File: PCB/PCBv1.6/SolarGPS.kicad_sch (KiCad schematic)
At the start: 46 parts, among them J1 Conn_01x10_Female, J2 Solar2+, J3 Solar1+, J4 GND, J5 GND, J6 Conn_02x03_Odd_Even, J7 Screw_Terminal_01x01, J8 Conn_01x04_Male, U1 BQ25505, U2 MAX-M10Q, U3 STM32L031G6Ux, U4 MAX40200AUK, U6 LIS3DH, Y1 32.768

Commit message: More Progress
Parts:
- removed D2: LED, Diode_SMD:D_0805_2012Metric, symbol Device:LED
- removed R2, R3: 100, Resistor_SMD:R_0603_1608Metric, symbol Device:R_Small
- removed U2: MAX-M10Q, RF_GPS:ublox_MAX, symbol RF_GPS:MAX-M8Q
- added U2: MAX-M10S, Margo_Lib:MAX-8, symbol MargoGeneral:MAX-M10S
- C8: symbol Device:CP -> Device:C_Polarized
- U1: footprint Package_DFN_QFN:QFN-20-1EP_3.5x3.5mm_P0.5mm_EP2x2mm -> Package_DFN_QFN:Texas_VQFN-RGR-20
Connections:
- net GND: now also U2.1 (GND), U2.10 (GND), U2.12 (GND)
- net GPS_EN: now also U3.10 (PA4); no longer U3.24 (PB3)
- net GPS_EXINT: now also U2.5 (EXINT)
- net GPS_RF: now also U2.11 (RF_IN)
- net GPS_UART_MISO: now also U2.2 (TXD)
- net GPS_UART_MOSI: now also U2.3 (RXD)
- net GPS_VDD: now also U2.7 (VCC_IO), U2.8 (VCC)
- net VBAT_OK: now also J1.5 (Pin_5)
- net VDD: now also U2.6 (V_BCKP)
- net DISPEN: no longer names the net of U3.18 (PA8)
- net DISPEN: no longer J1.5 (Pin_5)
- net LED: no longer names the net of U3.19 (PA9)
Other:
- note added: "Pin 5: LCD Enable"
- moved on the sheet: AE1, C1, C2, C5, J8, R4, U4

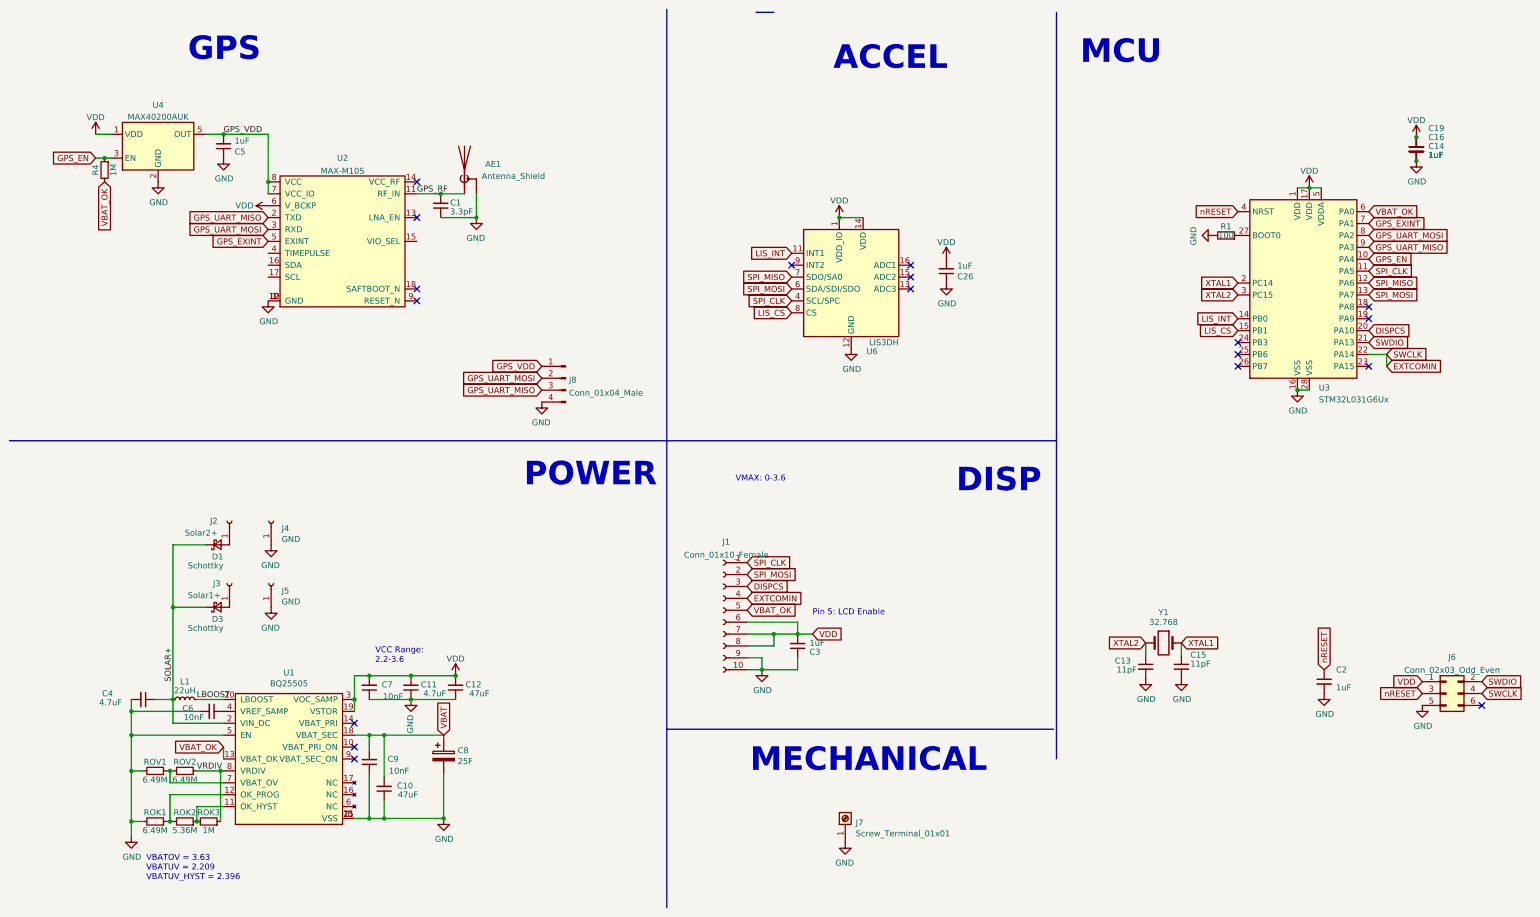
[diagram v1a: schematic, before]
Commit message: Replace GNSS with L96
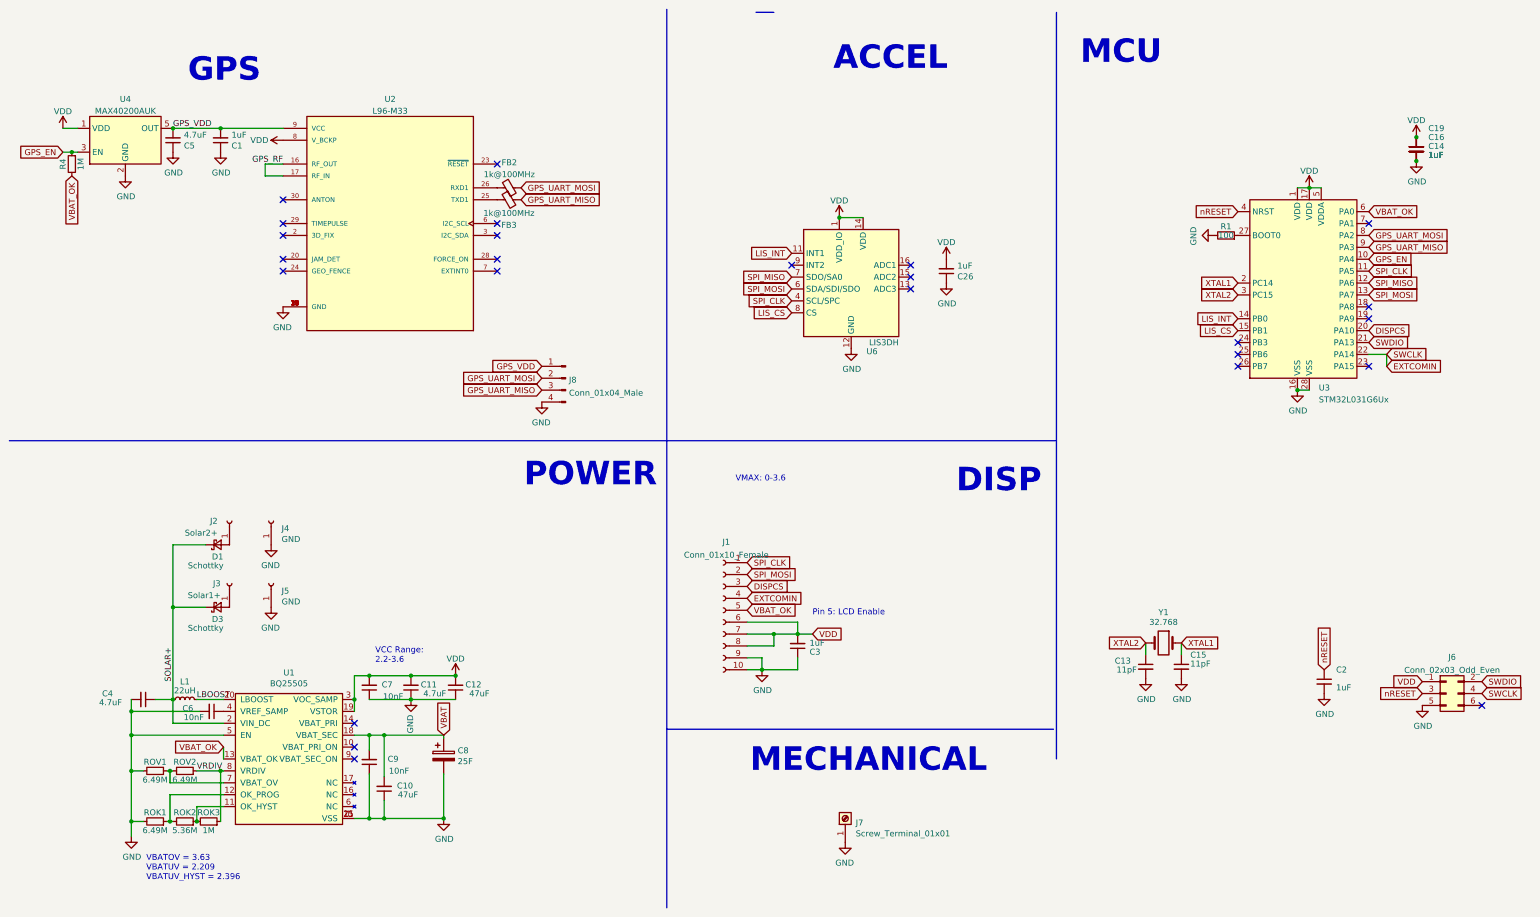
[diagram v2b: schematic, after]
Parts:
- removed AE1: Antenna_Shield, RF_Antenna:Pulse_W3011, symbol Device:Antenna_Shield
- removed U2: MAX-M10S, Margo_Lib:MAX-8, symbol MargoGeneral:MAX-M10S
- added FB2, FB3: 1k@100MHz, Resistor_SMD:R_0603_1608Metric, symbol Device:FerriteBead_Small
- added U2: L96-M33, XCVR_L96-M33, symbol Heliograph:L96-M33
- C1: value 3.3pF -> 1uF; footprint Capacitor_SMD:C_0402_1005Metric -> Capacitor_SMD:C_0603_1608Metric
- C5: value 1uF -> 4.7uF; footprint Capacitor_SMD:C_0603_1608Metric -> Capacitor_SMD:C_0805_2012Metric
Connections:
- net GND: now also U2.10 (GND), U2.11 (GND), U2.12 (GND), U2.13 (GND), U2.14 (GND), U2.15 (GND), U2.18 (GND), U2.19 (GND), U2.21 (GND), U2.22 (GND), U2.27 (GND), U2.31 (GND), U2.4 (GND), U2.5 (GND)
- net GPS_RF: now also U2.16 (RF_OUT), U2.17 (RF_IN); no longer C1.2
- net GPS_UART_MISO: now also FB3.2
- net GPS_UART_MOSI: now also FB2.1
- net GPS_VDD: now also C1.2, U2.9 (VCC)
- net VDD: now also U2.8 (V_BCKP)
- net GPS_EXINT: no longer names the net of U3.7 (PA1)
- new net: FB3.1, U2.25 (TXD1)
- new net: FB2.2, U2.26 (RXD1)
- no-connect marks 18 -> 25
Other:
- moved on the sheet: C5, R4, U4

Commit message: Update PCBV10
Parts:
- removed C11, C4: 4.7uF, Capacitor_SMD:C_0805_2012Metric, symbol Device:C_Small
- removed C12: 47uF, Capacitor_SMD:C_1206_3216Metric, symbol Device:C_Small
- removed C8: 25F, Heliograph:TPLC3R8-25MR8X20, symbol Device:C_Polarized
- removed D3: Schottky, Diode_SMD:D_SOD-323_HandSoldering, symbol Device:D_Schottky_Small
- removed ROK1, ROV1, ROV2: 6.49M, Resistor_SMD:R_0603_1608Metric, symbol Device:R_Small
- removed ROK2: 5.36M, Resistor_SMD:R_0603_1608Metric, symbol Device:R_Small
- removed ROK3: 1M, Resistor_SMD:R_0603_1608Metric, symbol Device:R_Small
- removed U1: BQ25505, Package_DFN_QFN:Texas_VQFN-RGR-20, symbol MargoGeneral:BQ25505
- added C4: 25F, Heliograph:TPLC3R8-25MR8X20, symbol Device:C_Polarized
- added C8: 10nF, Capacitor_SMD:C_0603_1608Metric, symbol Device:C_Small
- added D2: Schottky, Diode_SMD:D_SOD-323_HandSoldering, symbol Device:D_Schottky_Small
- added R2, R3: 1M, Resistor_SMD:R_0603_1608Metric, symbol Device:R_Small
- added R6: 432k, Resistor_SMD:R_0603_1608Metric, symbol Device:R_Small
- added R7: 86k, Resistor_SMD:R_0603_1608Metric, symbol Device:R_Small
- added U1: TPS63802, Margo_Lib:VREG_TPS63802DLAR, symbol SolarGPS-rescue:TPS63802-VeridianDesigns
- C6: value 10nF -> 1uF
- C7: value 10nF -> 0.1uF
- C9: value 10nF -> 47uF; footprint Capacitor_SMD:C_0603_1608Metric -> Capacitor_SMD:C_1206_3216Metric
- J2: value Solar2+ -> GND
- J3: value Solar1+ -> GND
- J4: value GND -> Solar1+
- J5: value GND -> Solar2+
- L1: value 22uH -> 0.47uH; footprint Heliograph:744031220 -> Inductor_SMD:L_0805_2012Metric_Pad1.05x1.20mm_HandSolder; Part 744031220 -> DFE201612E
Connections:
- net GND: now also C6.1, J2.1 (Pin_1), J3.1 (Pin_1), R4.2, C4.2, C8.1, R3.2, R7.1, U1.2 (MODE), U1.3 (AGND), U1.8 (GND); no longer C6.2, J4.1 (Pin_1), J5.1 (Pin_1)
- net VBAT: now also C6.2, D1.1 (K), C4.1, D2.1 (K), R2.1, U1.10 (VIN); no longer C9.2
- net VDD: now also C9.2, J1.5 (Pin_5), C8.2, R6.2, U1.6 (VOUT); no longer C7.2
- net VBATSENSE: now reaches U3.7 (PA1)
- net VBATSENSE: now also C7.2, R2.2, R3.1, U1.1 (EN)
- net SOLAR1+: now reaches D1.2 (A)
- net SOLAR1+: now also J4.1 (Pin_1); no longer J2.1 (Pin_1)
- net LBOOST: no longer names the net of L1.2
- net LBOOST: now also U1.7 (L2)
- net SOLAR+: no longer names the net of L1.1
- net SOLAR+: now also U1.9 (L1); no longer D1.1 (K)
- removed net VBAT_OK: J1.5 (Pin_5), R4.2, U3.6 (PA0)
- new net FB: R6.1, R7.2, U1.4 (FB)
- new net SOLAR2+: D2.2 (A), J5.1 (Pin_1)
- no-connect marks 25 -> 23
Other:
- note added: "VOUT = 3.01"
- note removed: "VBATOV = 3.63 VBATUV = 2.209 VBATUV_HYST = 2.396"
- note removed: "VCC Range: 2.2-3.6"
- note removed: "VMAX: 0-3.6"

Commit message: PCB1.6
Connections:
- net DISPCS: now also U3.19 (PA9); no longer U3.20 (PA10)
- net GND: now also J1.8 (Pin_8)
- net VDD: no longer J1.5 (Pin_5), J1.8 (Pin_8)
- net EXTCOMIN renamed SWCLK
- net SWCLK: no longer J1.4 (Pin_4)
- new net LCDEN: J1.5 (Pin_5), U3.20 (PA10)
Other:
- note added: "Pin 4: EXTIN Pin 5: LCD Enable Pin 8: EXTMODE H=Hardware, L=Software"
- note removed: "Pin 5: LCD Enable"
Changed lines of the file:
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@@
   (junction (at 66.04 153.035) (diameter 0) (color 0 0 0 0)
   )
-  (junction (at 180.34 142.24) (diameter 0) (color 0 0 0 0)
-  )
   (junction (at 57.15 36.83) (diameter 0) (color 0 0 0 0)
   )
@@
   (junction (at 85.09 163.195) (diameter 0) (color 0 0 0 0)
   )
+  (junction (at 172.72 149.86) (diameter 0) (color 0 0 0 0)
+  )
   (junction (at 66.04 165.735) (diameter 0) (color 0 0 0 0)
   )
@@
   (junction (at 119.38 165.735) (diameter 0) (color 0 0 0 0)
   )
-  (junction (at 175.26 144.78) (diameter 0) (color 0 0 0 0)
-  )
   (junction (at 46.99 46.99) (diameter 0) (color 0 0 0 0)
   )
-  (no_connect (at 302.26 77.47))
+  (no_connect (at 169.545 137.16))
   (no_connect (at 204.47 71.12))
   (no_connect (at 107.315 155.575))
@@
     (stroke (width 0) (type default) (color 0 0 0 0))
   )
-  (wire (pts (xy 180.34 139.7) (xy 169.545 139.7))
-    (stroke (width 0) (type default) (color 0 0 0 0))
-  )
   (wire (pts (xy 172.72 149.86) (xy 172.72 152.4))
     (stroke (width 0) (type default) (color 0 0 0 0))
@@
     (stroke (width 0) (type default) (color 0 0 0 0))
   )
-  (wire (pts (xy 175.26 147.32) (xy 175.26 144.78))
+  (wire (pts (xy 172.72 149.86) (xy 172.72 147.32))
     (stroke (width 0) (type default) (color 0 0 0 0))
   )
@@
     (stroke (width 0) (type default) (color 0 0 0 0))
   )
+  (wire (pts (xy 172.72 147.32) (xy 169.545 147.32))
+    (stroke (width 0) (type default) (color 0 0 0 0))
+  )
   (polyline (pts (xy 12.065 103.505) (xy 235.585 103.505))
     (stroke (width 0) (type default) (color 0 0 0 0))
@@
     (stroke (width 0) (type default) (color 0 0 0 0))
   )
-  (wire (pts (xy 169.545 147.32) (xy 175.26 147.32))
-    (stroke (width 0) (type default) (color 0 0 0 0))
-  )
   (wire (pts (xy 85.09 163.195) (xy 86.995 163.195))
     (stroke (width 0) (type default) (color 0 0 0 0))
@@
     (stroke (width 0) (type default) (color 0 0 0 0))
   )
-  (wire (pts (xy 169.545 144.78) (xy 175.26 144.78))
+  (wire (pts (xy 169.545 144.78) (xy 180.34 144.78))
     (stroke (width 0) (type default) (color 0 0 0 0))
   )
@@
     (stroke (width 0) (type default) (color 0 0 0 0))
   )
-  (wire (pts (xy 180.34 142.24) (xy 180.34 139.7))
-    (stroke (width 0) (type default) (color 0 0 0 0))
-  )
   (wire (pts (xy 25.4 46.99) (xy 36.83 46.99))
     (stroke (width 0) (type default) (color 0 0 0 0))
   )
-  (wire (pts (xy 175.26 144.78) (xy 180.34 144.78))
-    (stroke (width 0) (type default) (color 0 0 0 0))
-  )
   (wire (pts (xy 85.09 163.195) (xy 85.09 165.735))
     (stroke (width 0) (type default) (color 0 0 0 0))
@@
     (stroke (width 0) (type default) (color 0 0 0 0))
   )
-  (wire (pts (xy 302.26 85.09) (xy 306.07 85.09))
-    (stroke (width 0) (type default) (color 0 0 0 0))
-  )
   (wire (pts (xy 36.83 46.99) (xy 46.99 46.99))
     (stroke (width 0) (type default) (color 0 0 0 0))
@@
   )
   (wire (pts (xy 107.315 153.035) (xy 116.205 153.035))
-    (stroke (width 0) (type default) (color 0 0 0 0))
-  )
-  (wire (pts (xy 306.07 87.63) (xy 306.07 85.09))
     (stroke (width 0) (type default) (color 0 0 0 0))
   )
@@
     (effects (font (size 5.0038 5.0038) (thickness 1.0008) bold) (justify left bottom))
   )
-  (text "Pin 5: LCD Enable" (at 183.515 140.97 0)
+  (text "Pin 4: EXTIN\nPin 5: LCD Enable\nPin 8: EXTMODE H=Hardware, L=Software"
+    (at 189.23 138.43 0)
     (effects (font (size 1.27 1.27)) (justify left bottom))
   )
@@
     )
   )
+  (global_label "LCDEN" (shape input) (at 302.26 80.01 0) (fields_autoplaced)
+    (effects (font (size 1.27 1.27)) (justify left))
+    (property "Intersheet References" "${INTERSHEET_REFS}" (id 0) (at 310.6318 79.9306 0)
+      (effects (font (size 1.27 1.27)) (justify left) hide)
+    )
+  )
   (global_label "GPS_UART_MISO" (shape input) (at 121.285 52.07 0) (fields_autoplaced)
     (effects (font (size 1.27 1.27)) (justify left))
@@
     )
   )
-  (global_label "DISPCS" (shape input) (at 302.26 80.01 0) (fields_autoplaced)
-    (effects (font (size 1.27 1.27)) (justify left))
-    (property "Intersheet References" "${INTERSHEET_REFS}" (id 0) (at 311.418 79.9306 0)
+  (global_label "DISPCS" (shape input) (at 302.26 77.47 0) (fields_autoplaced)
+    (effects (font (size 1.27 1.27)) (justify left))
+    (property "Intersheet References" "${INTERSHEET_REFS}" (id 0) (at 311.418 77.3906 0)
       (effects (font (size 1.27 1.27)) (justify left) hide)
     )
@@
     )
   )
-  (global_label "EXTCOMIN" (shape input) (at 306.07 87.63 0) (fields_autoplaced)
-    (effects (font (size 1.27 1.27)) (justify left))
-    (property "Intersheet References" "${INTERSHEET_REFS}" (id 0) (at 317.7075 87.5506 0)
-      (effects (font (size 1.27 1.27)) (justify left) hide)
-    )
-  )
   (global_label "SWDIO" (shape input) (at 302.26 82.55 0) (fields_autoplaced)
     (effects (font (size 1.27 1.27)) (justify left))
@@
     )
   )
-  (global_label "EXTCOMIN" (shape input) (at 169.545 137.16 0) (fields_autoplaced)
-    (effects (font (size 1.27 1.27)) (justify left))
-    (property "Intersheet References" "${INTERSHEET_REFS}" (id 0) (at 181.1825 137.0806 0)
-      (effects (font (size 1.27 1.27)) (justify left) hide)
-    )
-  )
   (global_label "SPI_MOSI" (shape input) (at 169.545 132.08 0) (fields_autoplaced)
     (effects (font (size 1.27 1.27)) (justify left))
@@
     )
   )
-  (global_label "SWCLK" (shape input) (at 306.07 85.09 0) (fields_autoplaced)
-    (effects (font (size 1.27 1.27)) (justify left))
-    (property "Intersheet References" "${INTERSHEET_REFS}" (id 0) (at 314.6232 85.0106 0)
+  (global_label "SWCLK" (shape input) (at 302.26 85.09 0) (fields_autoplaced)
+    (effects (font (size 1.27 1.27)) (justify left))
+    (property "Intersheet References" "${INTERSHEET_REFS}" (id 0) (at 310.8132 85.0106 0)
       (effects (font (size 1.27 1.27)) (justify left) hide)
     )
@@
     (property "Intersheet References" "${INTERSHEET_REFS}" (id 0) (at 246.8075 146.6056 0)
       (effects (font (size 1.27 1.27)) (justify right) hide)
+    )
+  )
+  (global_label "LCDEN" (shape input) (at 169.545 139.7 0) (fields_autoplaced)
+    (effects (font (size 1.27 1.27)) (justify left))
+    (property "Intersheet References" "${INTERSHEET_REFS}" (id 0) (at 177.9168 139.6206 0)
+      (effects (font (size 1.27 1.27)) (justify left) hide)
     )
   )
@@
   )
   (symbol (lib_id "Connector:Conn_01x10_Female") (at 164.465 139.7 0) (mirror y) (unit 1)
-    (in_bom yes) (on_board yes) (fields_autoplaced)
-    (property "Reference" "J1" (id 0) (at 165.1 125.1163 0))
-    (property "Value" "Conn_01x10_Female" (id 1) (at 165.1 127.8914 0))
+    (in_bom yes) (on_board yes)
+    (property "Reference" "J1" (id 0) (at 165.1 124.46 0))
+    (property "Value" "Conn_01x10_Female" (id 1) (at 173.355 126.365 0))
     (property "Footprint" "Heliograph:LS013B7DH03" (id 2) (at 164.465 139.7 0)
       (effects (font (size 1.27 1.27)) hide)
